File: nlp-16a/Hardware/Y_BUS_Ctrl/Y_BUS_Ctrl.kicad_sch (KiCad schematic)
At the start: 0 parts

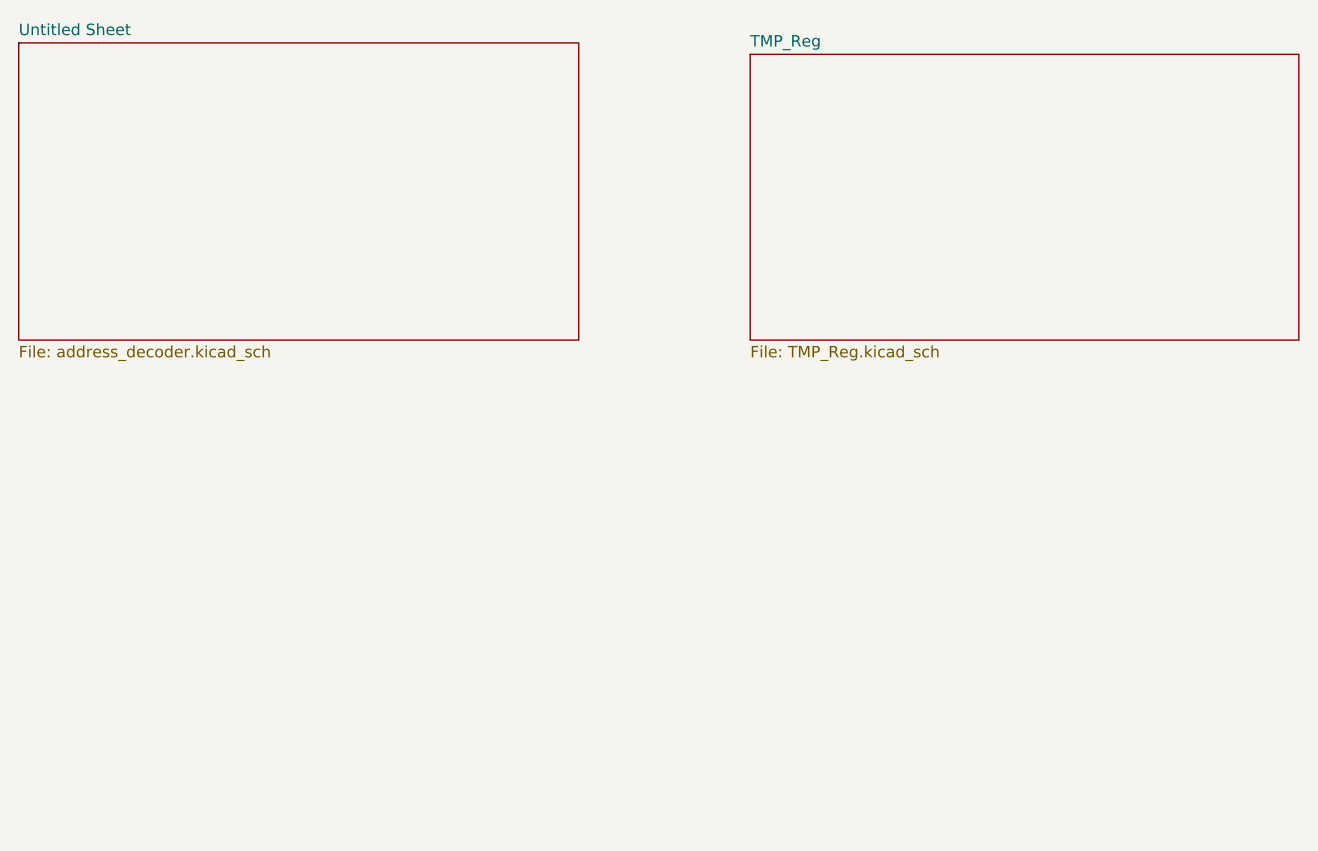
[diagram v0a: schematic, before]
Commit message: TMPレジスタ等を追加
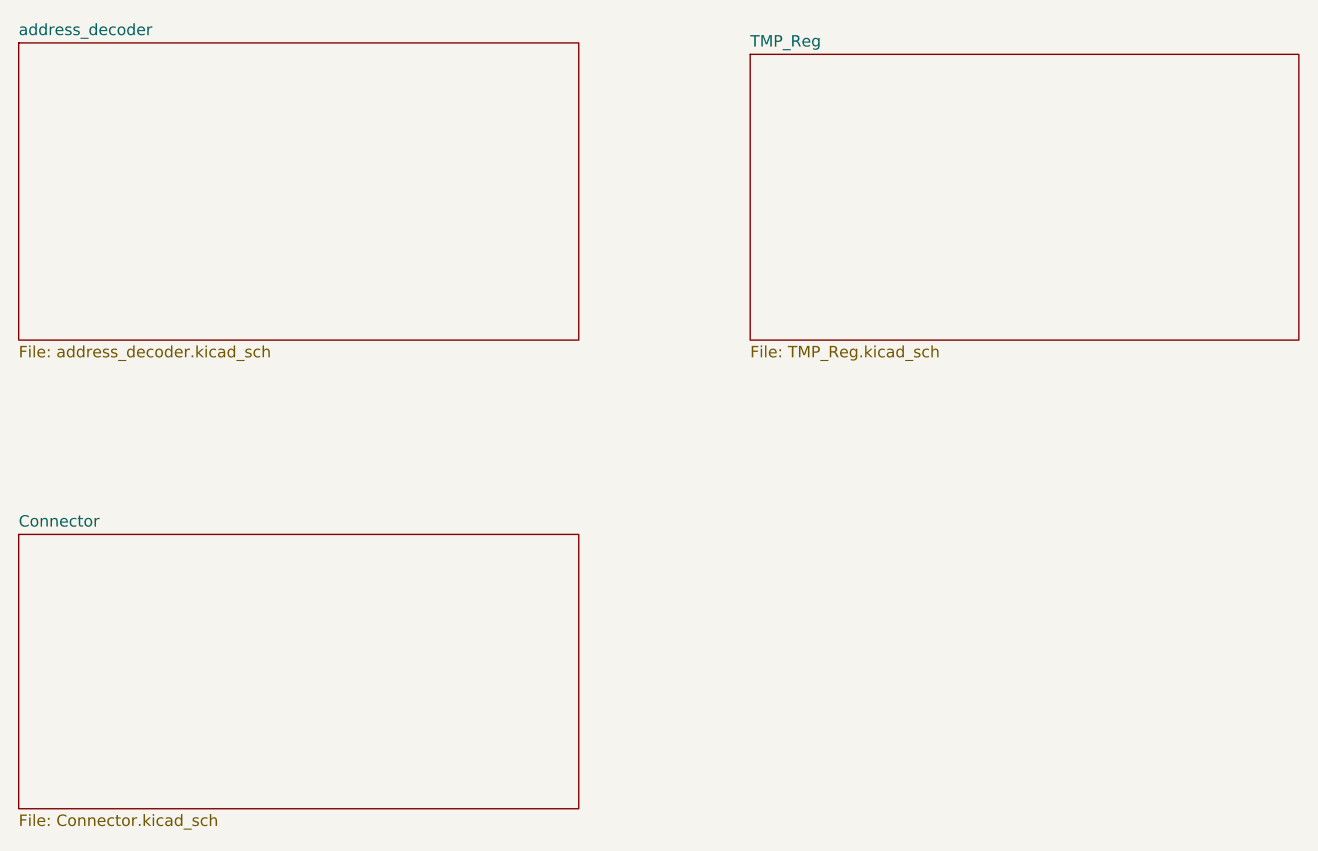
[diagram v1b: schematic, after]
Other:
- sheet Untitled Sheet renamed address_decoder
- added sheet Connector (Connector.kicad_sch)
